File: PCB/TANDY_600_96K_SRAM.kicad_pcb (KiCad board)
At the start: 2 copper layers, 68.6 x 45.1 mm, 7 parts, among them J1 DIN-41612-44-M-RA, U1 628128, U2 74HC148

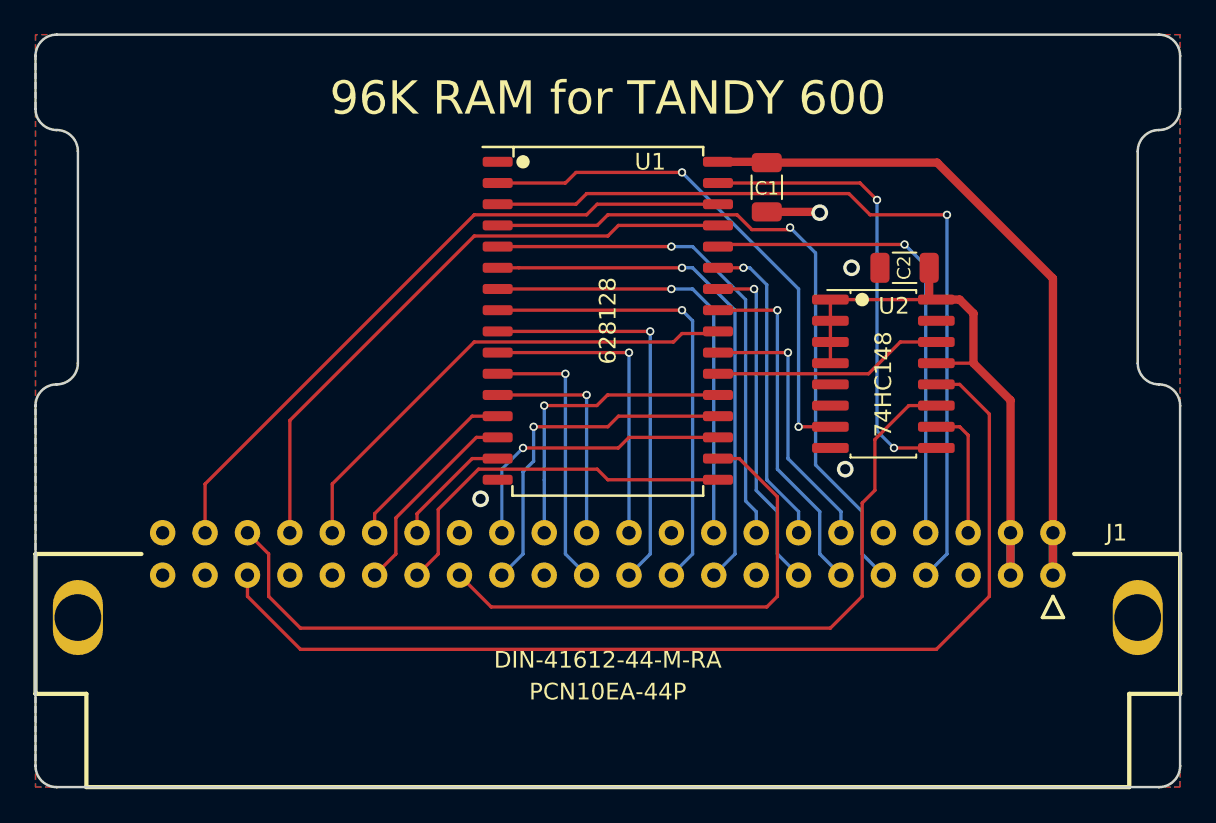
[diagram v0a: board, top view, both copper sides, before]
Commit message: datasheets, update bom, teardrops on release gerbers
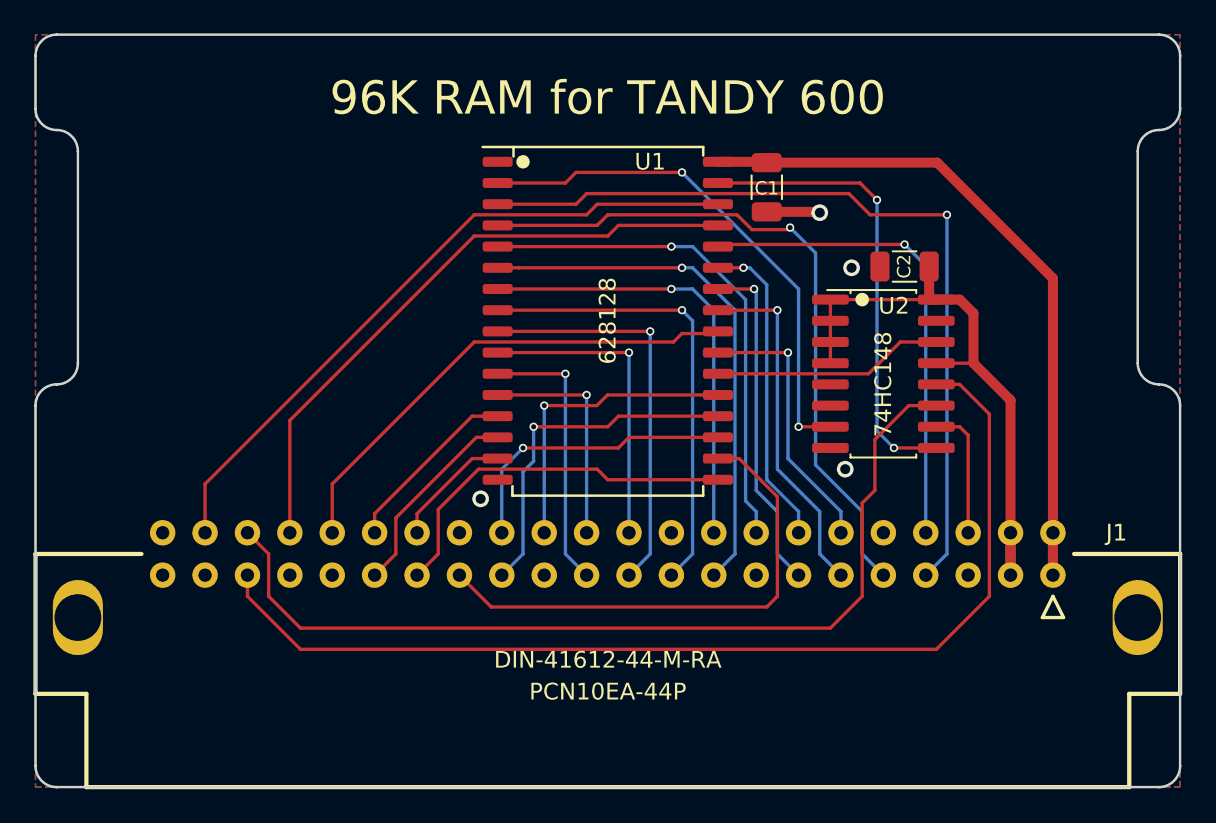
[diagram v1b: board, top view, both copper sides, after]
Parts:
- moved C2 0.08 mm to (163.8, 106.0)
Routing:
- net /~{WE}: track 37.9 -> 37.2 mm
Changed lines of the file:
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@@
   (title_block
     (title "TANDY 600 96K SRAM")
-    (date "2022-09-08")
-    (rev "007")
+    (date "2022-09-16")
+    (rev "008")
     (company "Brian K. White - b.kenyon.w@gmail.com")
     (comment 1 "LICENSE: CC-BY-SA 4.0")
@@
   )
   (setup
+    (stackup
+      (layer "F.SilkS" (type "Top Silk Screen"))
+      (layer "F.Paste" (type "Top Solder Paste"))
+      (layer "F.Mask" (type "Top Solder Mask") (thickness 0.01))
+      (layer "F.Cu" (type "copper") (thickness 0.035))
+      (layer "dielectric 1" (type "core") (thickness 1.51) (material "FR4") (epsilon_r 4.5) (loss_tangent 0.02))
+      (layer "B.Cu" (type "copper") (thickness 0.035))
+      (layer "B.Mask" (type "Bottom Solder Mask") (thickness 0.01))
+      (layer "B.Paste" (type "Bottom Solder Paste"))
+      (layer "B.SilkS" (type "Bottom Silk Screen"))
+      (copper_finish "None")
+      (dielectric_constraints no)
+    )
     (pad_to_mask_clearance 0)
     (solder_mask_min_width 0.22)
@@
   )
   (footprint "000_LOCAL:C_1206" (layer "F.Cu")
-    (at 163.83 106.045 180)
+    (at 163.83 105.9688 180)
     (descr "Capacitor SMD 1206 (3216 Metric), square (rectangular) end terminal, IPC_7351 nominal, (Body size source: IPC-SM-782 page 76, https://www.pcb-3d.com/wordpress/wp-content/uploads/ipc-sm-782a_amendment_1_and_2.pdf), generated with kicad-footprint-generator")
     (tags "capacitor")
@@
     (effects (font (size 1.5 1.5) (thickness 0.15)))
   )
-  (segment (start 158.701 102.694) (end 158.75 102.743) (width 0.5) (layer "F.Cu") (net 1))
-  (segment (start 155.575 102.694) (end 158.701 102.694) (width 0.5) (layer "F.Cu") (net 1))
+  (segment (start 155.575 102.694) (end 158.701 102.694) (width 0.6) (layer "F.Cu") (net 1))
+  (segment (start 158.701 102.694) (end 158.75 102.743) (width 0.6) (layer "F.Cu") (net 1))
   (via (at 138.43 119.888) (size 1) (drill 0.6) (layers "F.Cu" "B.Cu") (net 1))
   (via (at 160.274 118.11) (size 1) (drill 0.6) (layers "F.Cu" "B.Cu") (net 1))
   (via (at 160.655 106.045) (size 1) (drill 0.6) (layers "F.Cu" "B.Cu") (net 1))
   (via (at 158.75 102.743) (size 1) (drill 0.6) (layers "F.Cu" "B.Cu") (net 1))
-  (segment (start 165.784 99.744) (end 155.575 99.744) (width 0.5) (layer "F.Cu") (net 2))
+  (segment (start 165.784 99.744) (end 155.575 99.744) (width 0.6) (layer "F.Cu") (net 2))
   (segment (start 155.575 99.744) (end 155.526 99.695) (width 0.5) (layer "F.Cu") (net 2))
-  (segment (start 172.72 106.68) (end 165.784 99.744) (width 0.5) (layer "F.Cu") (net 2))
-  (segment (start 155.526 99.695) (end 152.65 99.695) (width 0.5) (layer "F.Cu") (net 2))
-  (segment (start 172.72 124.46) (end 172.72 121.92) (width 0.5) (layer "F.Cu") (net 2))
-  (segment (start 172.72 121.92) (end 172.72 106.68) (width 0.5) (layer "F.Cu") (net 2))
-  (segment (start 172.72 121.92) (end 172.72 124.46) (width 0.5) (layer "B.Cu") (net 2))
-  (segment (start 170.18 113.9825) (end 170.18 121.92) (width 0.5) (layer "F.Cu") (net 3))
-  (segment (start 167.9575 108.7755) (end 167.9575 111.76) (width 0.5) (layer "F.Cu") (net 3))
-  (segment (start 165.7335 107.95) (end 167.132 107.95) (width 0.5) (layer "F.Cu") (net 3))
+  (segment (start 172.72 106.68) (end 165.784 99.744) (width 0.6) (layer "F.Cu") (net 2))
+  (segment (start 155.526 99.695) (end 152.65 99.695) (width 0.6) (layer "F.Cu") (net 2))
+  (segment (start 172.72 124.46) (end 172.72 121.92) (width 0.6) (layer "F.Cu") (net 2))
+  (segment (start 172.72 121.92) (end 172.72 106.68) (width 0.6) (layer "F.Cu") (net 2))
+  (segment (start 172.72 121.92) (end 172.72 124.46) (width 0.6) (layer "B.Cu") (net 2))
+  (segment (start 170.18 113.9825) (end 170.18 121.92) (width 0.6) (layer "F.Cu") (net 3))
+  (segment (start 167.9575 108.7755) (end 167.9575 111.76) (width 0.6) (layer "F.Cu") (net 3))
+  (segment (start 165.7335 107.95) (end 167.132 107.95) (width 0.6) (layer "F.Cu") (net 3))
   (segment (start 159.3865 111.76) (end 159.3865 107.9515) (width 0.2) (layer "F.Cu") (net 3))
   (segment (start 159.385 107.95) (end 165.7335 107.95) (width 0.2) (layer "F.Cu") (net 3))
   (segment (start 165.7335 111.76) (end 167.9575 111.76) (width 0.2) (layer "F.Cu") (net 3))
-  (segment (start 165.305 107.95) (end 165.7335 107.95) (width 0.5) (layer "F.Cu") (net 3))
+  (segment (start 165.305 107.95) (end 165.7335 107.95) (width 0.6) (layer "F.Cu") (net 3))
   (segment (start 159.3865 107.9515) (end 159.385 107.95) (width 0.2) (layer "F.Cu") (net 3))
-  (segment (start 167.9575 111.76) (end 170.18 113.9825) (width 0.5) (layer "F.Cu") (net 3))
-  (segment (start 167.132 107.95) (end 167.9575 108.7755) (width 0.5) (layer "F.Cu") (net 3))
-  (segment (start 170.18 124.46) (end 170.18 121.92) (width 0.5) (layer "F.Cu") (net 3))
-  (segment (start 165.305 106.045) (end 165.305 107.95) (width 0.5) (layer "F.Cu") (net 3))
-  (segment (start 170.18 121.92) (end 170.18 124.46) (width 0.5) (layer "B.Cu") (net 3))
+  (segment (start 167.9575 111.76) (end 170.18 113.9825) (width 0.6) (layer "F.Cu") (net 3))
+  (segment (start 167.132 107.95) (end 167.9575 108.7755) (width 0.6) (layer "F.Cu") (net 3))
+  (segment (start 170.18 124.46) (end 170.18 121.92) (width 0.6) (layer "F.Cu") (net 3))
+  (segment (start 165.305 106.045) (end 165.305 107.95) (width 0.6) (layer "F.Cu") (net 3))
+  (segment (start 170.18 121.92) (end 170.18 124.46) (width 0.6) (layer "B.Cu") (net 3))
   (segment (start 144.145 102.235) (end 139.45 102.235) (width 0.2) (layer "F.Cu") (net 4))
   (segment (start 144.78 101.6) (end 144.145 102.235) (width 0.2) (layer "F.Cu") (net 4))
@@
   (segment (start 138.049 110.49) (end 149.987 110.49) (width 0.2) (layer "F.Cu") (net 27))
   (segment (start 129.54 121.92) (end 129.54 118.999) (width 0.2) (layer "F.Cu") (net 27))
+  (segment (start 152.65 103.505) (end 146.685 103.505) (width 0.2) (layer "F.Cu") (net 28))
+  (segment (start 146.685 103.505) (end 146.05 104.14) (width 0.2) (layer "F.Cu") (net 28))
   (segment (start 146.05 104.14) (end 138.049 104.14) (width 0.2) (layer "F.Cu") (net 28))
-  (segment (start 146.685 103.505) (end 146.05 104.14) (width 0.2) (layer "F.Cu") (net 28))
-  (segment (start 127 121.92) (end 127 121.285) (width 0.25) (layer "F.Cu") (net 28))
-  (segment (start 152.65 103.505) (end 146.685 103.505) (width 0.2) (layer "F.Cu") (net 28))
   (segment (start 138.049 104.14) (end 127 115.189) (width 0.2) (layer "F.Cu") (net 28))
   (segment (start 127 115.189) (end 127 121.92) (width 0.2) (layer "F.Cu") (net 28))

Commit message: silkscreen, symbols, footprints touchups
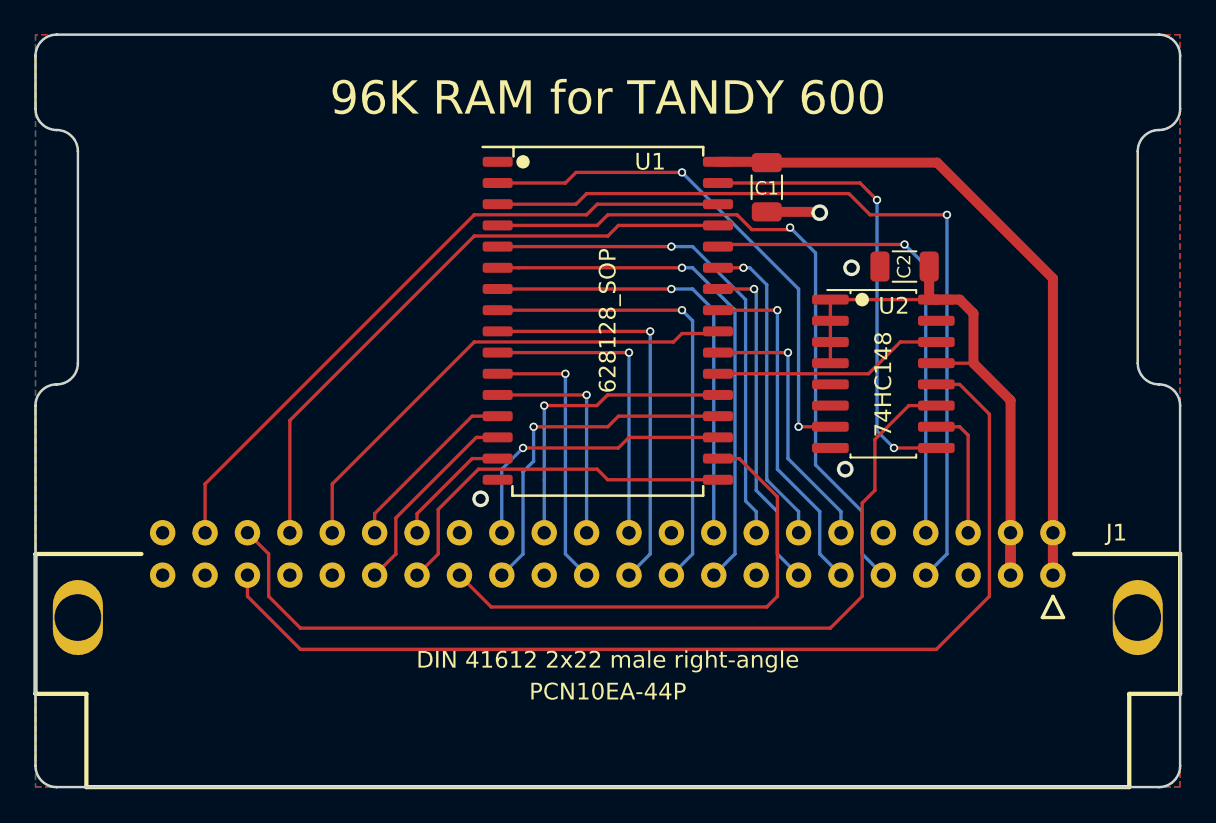
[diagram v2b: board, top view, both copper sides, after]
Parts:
- J1: value DIN-41612-44-M-RA -> DIN 41612 2x22 male right-angle; footprint 000_LOCAL:DIN41612-44P-male-horiz -> 000_LOCAL:DIN 41612 2x22 male right-angle
- U1: value 628128 -> 628128_SOP
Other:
- board text added: "1A"
- board text added: "1B"
- board text added: "22A"
- board text added: "22B"
- board text added: "enclosure top shell - card must be this tall to be secured"
- board text removed: "Top cover actual contact points and elevation."
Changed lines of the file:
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@@
       (effects (font (size 1 1) (thickness 0.15)))
     )
-    (fp_text value "628128" (at 0 0 -90) (layer "F.SilkS")
+    (fp_text value "628128_SOP" (at 0 0 -90) (layer "F.SilkS")
       (effects (font (size 1 1) (thickness 0.15)))
     )
@@
     )
   )
-  (footprint "000_LOCAL:DIN41612-44P-male-horiz" (layer "F.Cu")
+  (footprint "000_LOCAL:DIN 41612 2x22 male right-angle" (layer "F.Cu")
     (at 146.05 123.19)
     (property "Sheetfile" "TANDY_600_96K_SRAM.kicad_sch")
@@
       (effects (font (size 1 1) (thickness 0.15)))
     )
-    (fp_text value "DIN-41612-44-M-RA" (at 0 6.35) (layer "F.SilkS")
+    (fp_text value "DIN 41612 2x22 male right-angle" (at 0 6.35) (layer "F.SilkS")
       (effects (font (size 1 1) (thickness 0.15)))
     )
+    (fp_line (start -31.242 8.382) (end -34.29 8.382) (layer "F.SilkS") (width 0.254))
+    (fp_line (start -31.242 13.97) (end -31.242 8.382) (layer "F.SilkS") (width 0.254))
+    (fp_line (start 34.29 8.382) (end 31.242 8.382) (layer "F.SilkS") (width 0.254))
+    (fp_line (start 26.67 2.54) (end 26.035 3.81) (layer "F.SilkS") (width 0.2))
+    (fp_line (start 27.305 3.81) (end 26.67 2.54) (layer "F.SilkS") (width 0.2))
+    (fp_line (start 27.94 0) (end 34.29 0) (layer "F.SilkS") (width 0.254))
+    (fp_line (start 26.035 3.81) (end 27.305 3.81) (layer "F.SilkS") (width 0.2))
+    (fp_line (start 31.242 13.97) (end 31.242 8.382) (layer "F.SilkS") (width 0.254))
+    (fp_line (start -34.29 0) (end -34.29 8.382) (layer "F.SilkS") (width 0.254))
     (fp_line (start 34.29 0) (end 34.29 8.382) (layer "F.SilkS") (width 0.254))
-    (fp_line (start 26.67 2.54) (end 26.035 3.81) (layer "F.SilkS") (width 0.2))
+    (fp_line (start -27.94 0) (end -34.29 0) (layer "F.SilkS") (width 0.254))
     (fp_line (start 31.242 13.97) (end -31.242 13.97) (layer "F.SilkS") (width 0.254))
-    (fp_line (start 34.29 8.382) (end 31.242 8.382) (layer "F.SilkS") (width 0.254))
-    (fp_line (start 31.242 13.97) (end 31.242 8.382) (layer "F.SilkS") (width 0.254))
-    (fp_line (start -31.242 8.382) (end -34.29 8.382) (layer "F.SilkS") (width 0.254))
-    (fp_line (start 26.035 3.81) (end 27.305 3.81) (layer "F.SilkS") (width 0.2))
-    (fp_line (start 27.305 3.81) (end 26.67 2.54) (layer "F.SilkS") (width 0.2))
-    (fp_line (start -34.29 0) (end -34.29 8.382) (layer "F.SilkS") (width 0.254))
-    (fp_line (start -31.242 13.97) (end -31.242 8.382) (layer "F.SilkS") (width 0.254))
-    (fp_line (start 27.94 0) (end 34.29 0) (layer "F.SilkS") (width 0.254))
-    (fp_line (start -27.94 0) (end -34.29 0) (layer "F.SilkS") (width 0.254))
     (fp_line (start -28 7.57) (end 28 7.57) (layer "Dwgs.User") (width 0.15))
-    (pad "" thru_hole oval locked (at 31.75 3.81) (size 2.999999 4.500001) (drill 2.799999) (layers *.Cu *.Mask)
-      (net 1 "GND") (zone_connect 2))
-    (pad "" thru_hole oval locked (at -31.75 3.81) (size 2.999999 4.500001) (drill 2.799999) (layers *.Cu *.Mask)
-      (net 1 "GND") (zone_connect 2))
     (pad "1A" thru_hole circle (at 26.67 1.27) (size 1.524 1.524) (drill 0.8) (layers *.Cu *.Mask)
       (net 2 "VMEM") (pinfunction "1A") (pintype "passive"))
@@
     (pad "22B" thru_hole circle (at -26.67 -1.27) (size 1.524 1.524) (drill 0.8) (layers *.Cu *.Mask)
       (net 1 "GND") (pinfunction "22B") (pintype "passive"))
+    (pad "S1" thru_hole oval (at 31.75 3.81) (size 2.999999 4.500001) (drill 2.799999) (layers *.Cu *.Mask)
+      (net 1 "GND") (pinfunction "mount") (pintype "passive") (zone_connect 2))
+    (pad "S2" thru_hole oval (at -31.75 3.81) (size 2.999999 4.500001) (drill 2.799999) (layers *.Cu *.Mask)
+      (net 1 "GND") (pinfunction "mount") (pintype "passive") (zone_connect 2))
     (model "${KIPRJMOD}/000_LOCAL.pretty/3d/PCN10EA-44P.step"
       (offset (xyz 0 -7.30758 0))
@@
     (effects (font (size 1 1) (thickness 0.15)) (justify right mirror))
   )
+  (gr_text "1B" (at 173.99 121.92) (layer "B.SilkS")
+    (effects (font (size 1 1) (thickness 0.15)) (justify right mirror))
+  )
+  (gr_text "22B" (at 118.11 121.92) (layer "B.SilkS")
+    (effects (font (size 1 1) (thickness 0.15)) (justify left mirror))
+  )
   (gr_text "Originally based on Model600Sram_v1.1 by Jayeson Lee-Steere" (at 146.05 135.66) (layer "B.SilkS")
     (effects (font (size 1 1) (thickness 0.15)) (justify mirror))
@@
     (effects (font (size 1 1) (thickness 0.15)) (justify left mirror))
   )
+  (gr_text "22A" (at 118.11 124.46) (layer "B.SilkS")
+    (effects (font (size 1 1) (thickness 0.15)) (justify left mirror))
+  )
   (gr_text "${COMMENT2} v${REVISION}" (at 146.05 93.98) (layer "B.SilkS")
     (effects (font (size 1 1) (thickness 0.15)) (justify mirror))
   )
+  (gr_text "1A" (at 173.99 124.46) (layer "B.SilkS")
+    (effects (font (size 1 1) (thickness 0.15)) (justify right mirror))
+  )
   (gr_text "96K RAM for TANDY 600" (at 146.05 95.885) (layer "F.SilkS")
     (effects (font (size 2 2) (thickness 0.3)))
@@
     (effects (font (size 1 1) (thickness 0.15)))
   )
-  (gr_text "Top cover actual contact points and elevation." (at 146.05 90.17) (layer "Dwgs.User")
+  (gr_text "enclosure top shell - card must be this tall to be secured" (at 146.05 90.17) (layer "Dwgs.User")
     (effects (font (size 1.5 1.5) (thickness 0.15)))
   )
